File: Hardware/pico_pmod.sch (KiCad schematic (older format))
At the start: 8 parts, among them J1 Conn_02x15_Odd_Even, J2 Conn_01x02, J3 Conn_01x02, J4 Conn_01x02, J5 Conn_01x03, J6 Conn_01x02, J7 Conn_01x05, U1 Pico

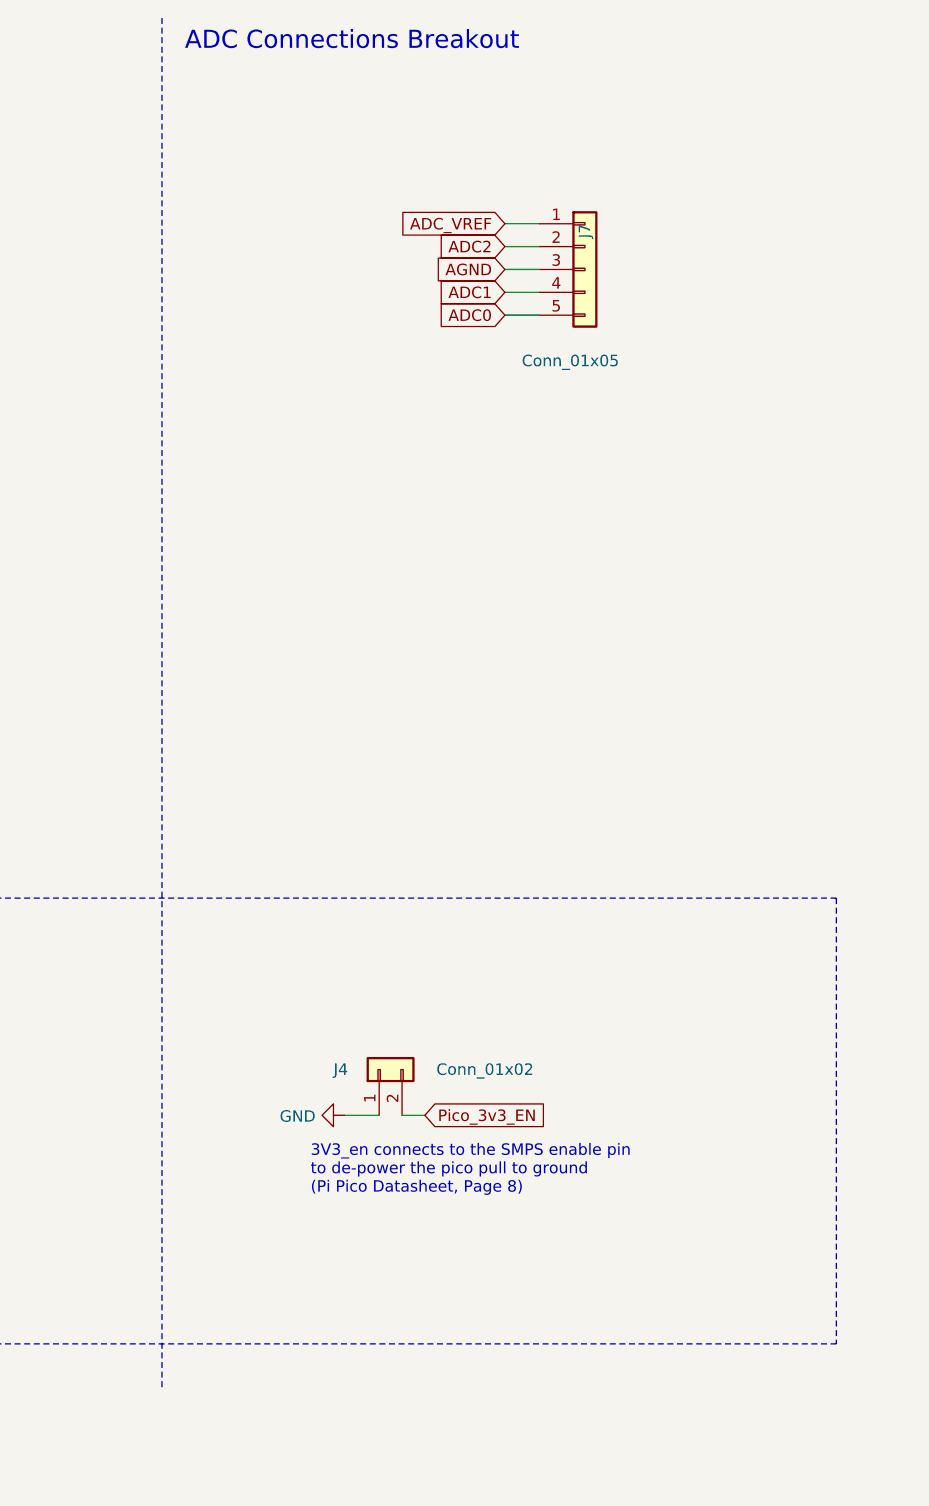
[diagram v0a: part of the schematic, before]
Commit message: Add Reset button to the Pico Schematic
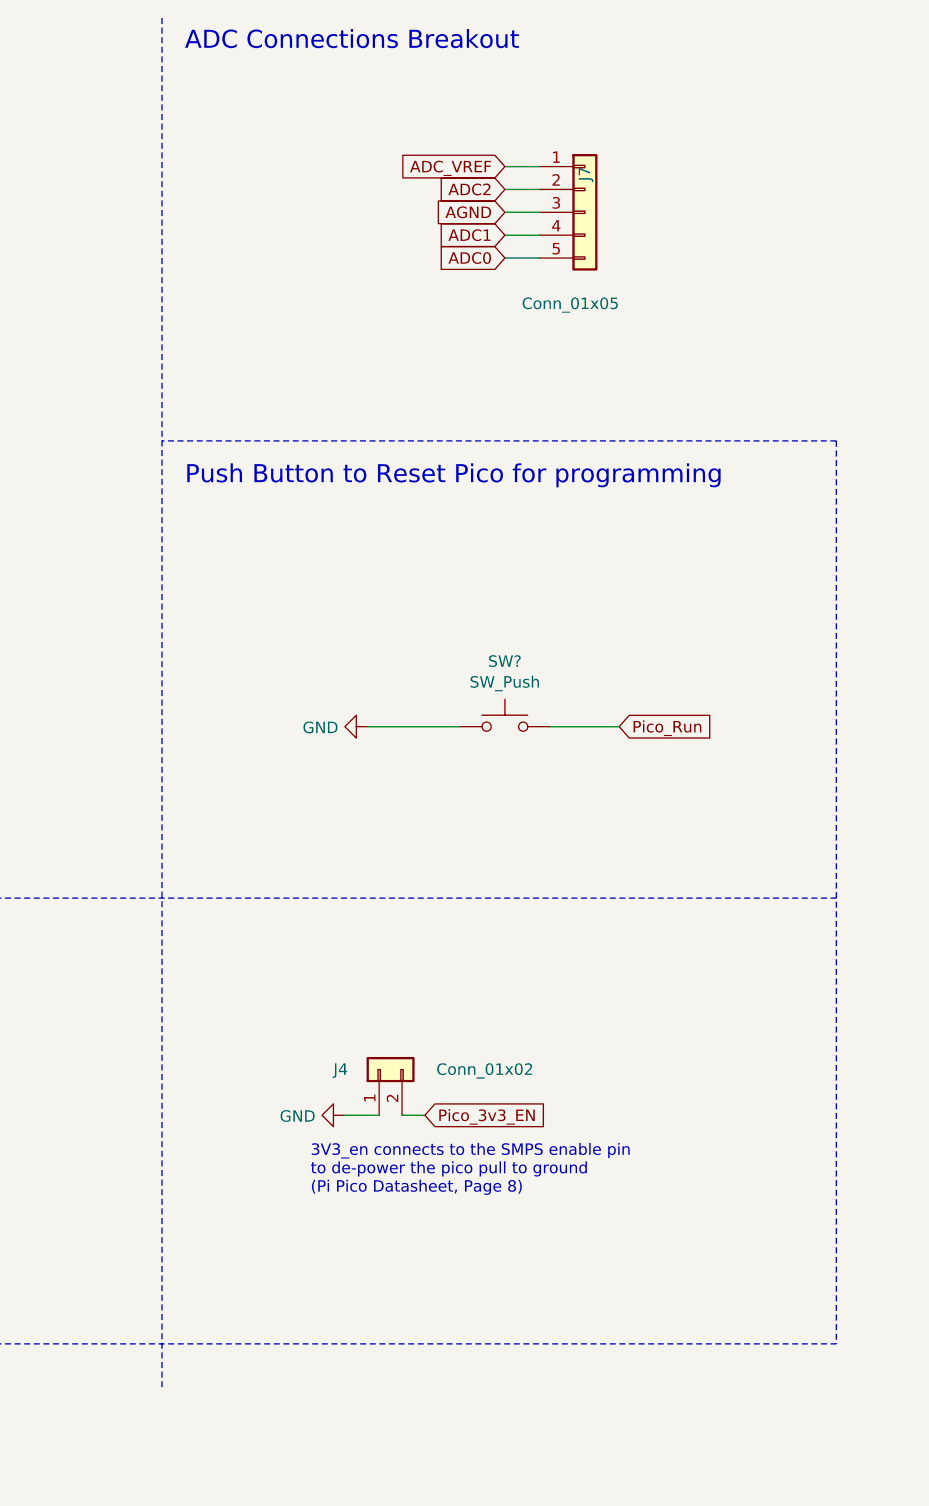
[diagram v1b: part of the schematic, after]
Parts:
- added SW?: SW_Push, Button_Switch_THT:SW_PUSH_6mm_H4.3mm, symbol Switch:SW_Push
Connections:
- net GND: now also SW?.1
- net Pico_Run: now also SW?.2
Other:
- note added: "Push Button to Reset Pico for programming"
- moved on the sheet: J7
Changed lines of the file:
@@
 L Connector_Generic:Conn_01x05 J7
 U 1 1 607A6E5A
-P 10050 1600
-F 0 "J7" V 10050 1800 50  0000 R CNN
-F 1 "Conn_01x05" H 10200 1200 50  0000 R CNN
-F 2 "Connector_PinHeader_2.54mm:PinHeader_1x05_P2.54mm_Vertical" H 10050 1600 50  0001 C CNN
-F 3 "~" H 10050 1600 50  0001 C CNN
-	1    10050 1600
+P 10050 1350
+F 0 "J7" V 10050 1550 50  0000 R CNN
+F 1 "Conn_01x05" H 10200 950 50  0000 R CNN
+F 2 "Connector_PinHeader_2.54mm:PinHeader_1x05_P2.54mm_Vertical" H 10050 1350 50  0001 C CNN
+F 3 "~" H 10050 1350 50  0001 C CNN
+	1    10050 1350
 	1    0    0    -1
 $EndComp
-Text GLabel 9700 1400 0    50   Input ~ 0
+Text GLabel 9700 1150 0    50   Input ~ 0
 ADC_VREF
-Text GLabel 9700 1500 0    50   Input ~ 0
+Text GLabel 9700 1250 0    50   Input ~ 0
 ADC2
-Text GLabel 9700 1600 0    50   Input ~ 0
+Text GLabel 9700 1350 0    50   Input ~ 0
 AGND
-Text GLabel 9700 1700 0    50   Input ~ 0
+Text GLabel 9700 1450 0    50   Input ~ 0
 ADC1
-Text GLabel 9700 1800 0    50   Input ~ 0
+Text GLabel 9700 1550 0    50   Input ~ 0
 ADC0
 Wire Wire Line
-	9700 1400 9850 1400
+	9700 1150 9850 1150
 Wire Wire Line
-	9700 1500 9850 1500
+	9700 1250 9850 1250
 Wire Wire Line
-	9700 1600 9850 1600
+	9700 1350 9850 1350
 Wire Wire Line
-	9850 1700 9700 1700
+	9850 1450 9700 1450
 Wire Wire Line
-	9700 1800 9850 1800
+	9700 1550 9850 1550
 Text GLabel 3300 1950 2    50   Input ~ 0
 ADC_VREF
@@
 	3300 2350 3050 2350
 Wire Notes Line
-	11150 4350 11150 6300
-Wire Notes Line
 	500  6300 11150 6300
 Wire Notes Line
@@
 Text Notes 8300 650  0    79   ~ 0
 ADC Connections Breakout\n
+$Comp
+L Switch:SW_Push SW?
+U 1 1 6081E990
+P 9700 3600
+F 0 "SW?" H 9700 3885 50  0000 C CNN
+F 1 "SW_Push" H 9700 3794 50  0000 C CNN
+F 2 "Button_Switch_THT:SW_PUSH_6mm_H4.3mm" H 9700 3800 50  0001 C CNN
+F 3 "~" H 9700 3800 50  0001 C CNN
+	1    9700 3600
+	1    0    0    -1
+$EndComp
+Text GLabel 10200 3600 2    50   Input ~ 0
+Pico_Run
+$Comp
+L power:GND #PWR?
+U 1 1 60823560
+P 9100 3600
+F 0 "#PWR?" H 9100 3350 50  0001 C CNN
+F 1 "GND" V 9105 3472 50  0000 R CNN
+F 2 "" H 9100 3600 50  0001 C CNN
+F 3 "" H 9100 3600 50  0001 C CNN
+	1    9100 3600
+	0    1    1    0
+$EndComp
+Wire Wire Line
+	9100 3600 9500 3600
+Wire Wire Line
+	9900 3600 10200 3600
+Wire Notes Line
+	11150 2350 8200 2350
+Wire Notes Line
+	11150 2350 11150 6300
+Text Notes 8300 2550 0    79   ~ 0
+Push Button to Reset Pico for programming
 $EndSCHEMATC

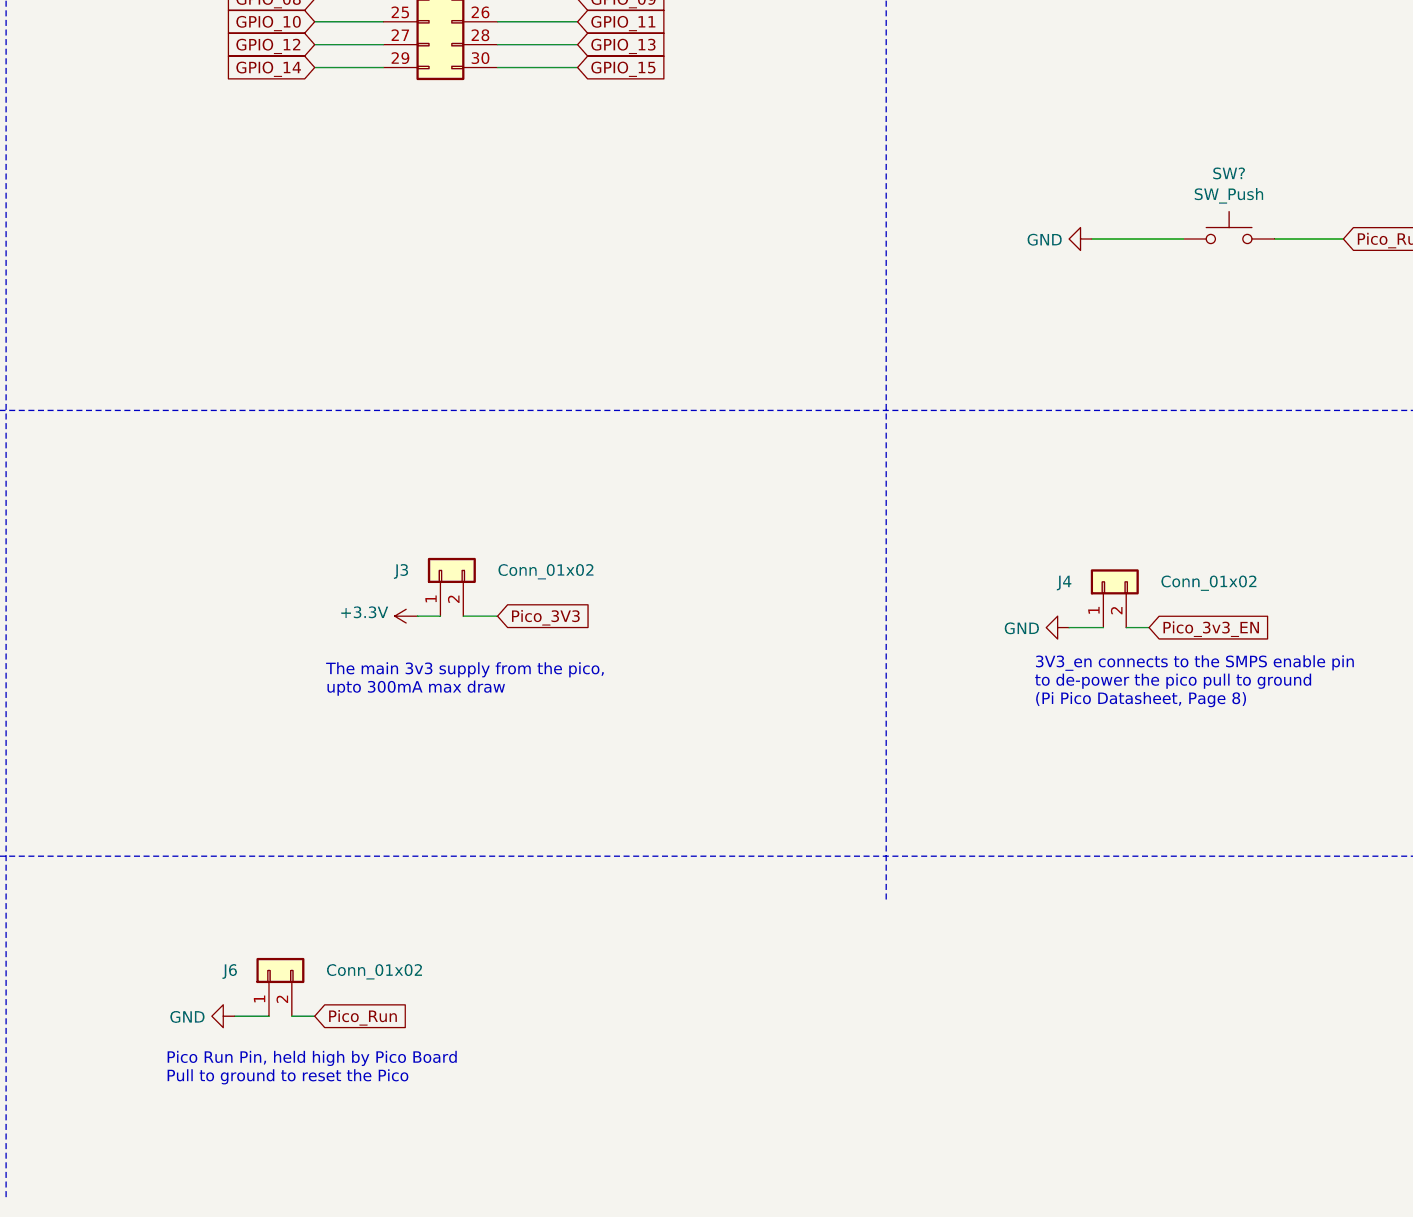
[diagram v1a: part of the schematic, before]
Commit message: Remove Run Header pins
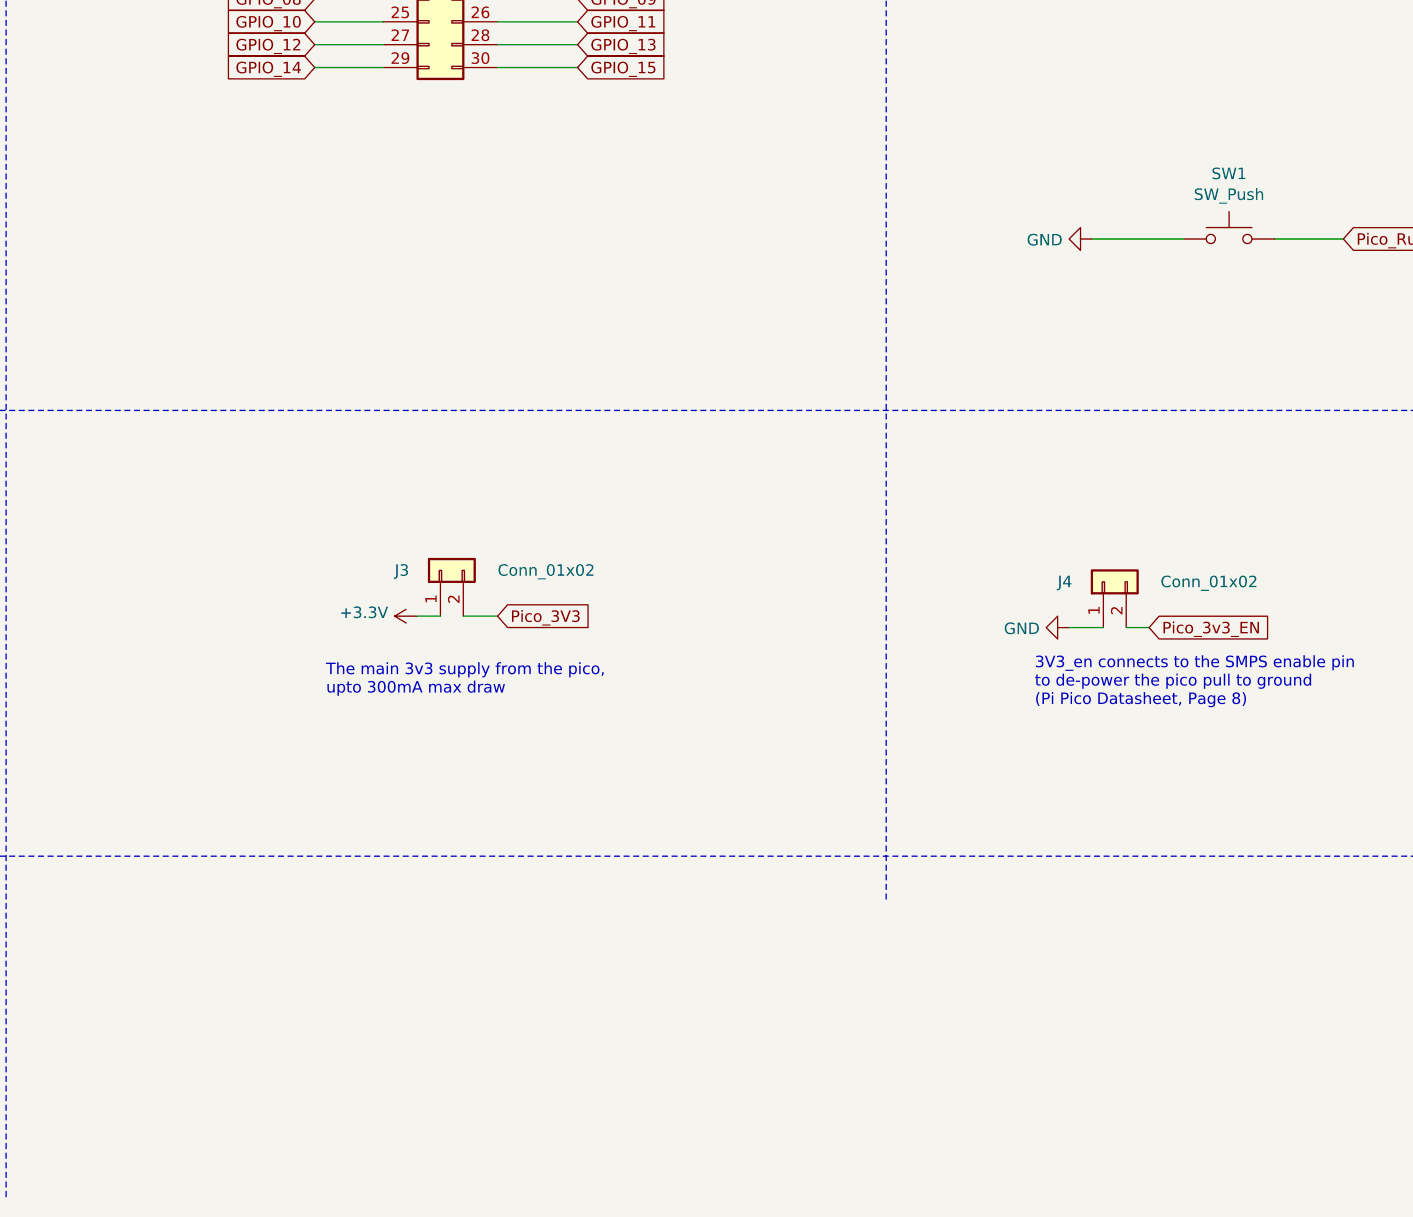
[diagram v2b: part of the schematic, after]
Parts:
- removed J6: Conn_01x02, Connector_PinHeader_2.54mm:PinHeader_1x02_P2.54mm_Vertical, symbol Connector_Generic:Conn_01x02
- gave numbers to parts that had none: 1
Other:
- note removed: "Pico Run Pin, held high by Pico Board\nPull to ground to reset the Pico"
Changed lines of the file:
@@
 Wire Wire Line
 	9150 5300 9000 5300
-Text GLabel 5700 7000 2    50   Input ~ 0
-Pico_Run
-$Comp
-L Connector_Generic:Conn_01x02 J6
-U 1 1 607985C4
-P 5500 6800
-F 0 "J6" V 5500 7000 50  0000 R CNN
-F 1 "Conn_01x02" V 5500 6550 50  0000 R CNN
-F 2 "Connector_PinHeader_2.54mm:PinHeader_1x02_P2.54mm_Vertical" H 5500 6800 50  0001 C CNN
-F 3 "~" H 5500 6800 50  0001 C CNN
-	1    5500 6800
-	0    -1   -1   0
-$EndComp
-Wire Wire Line
-	5600 7000 5700 7000
-Text Notes 5050 7300 0    50   ~ 0
-Pico Run Pin, held high by Pico Board\nPull to ground to reset the Pico
-$Comp
-L power:GND #PWR0124
-U 1 1 607985CC
-P 5350 7000
-F 0 "#PWR0124" H 5350 6750 50  0001 C CNN
-F 1 "GND" V 5355 6872 50  0000 R CNN
-F 2 "" H 5350 7000 50  0001 C CNN
-F 3 "" H 5350 7000 50  0001 C CNN
-	1    5350 7000
-	0    1    1    0
-$EndComp
-Wire Wire Line
-	5500 7000 5350 7000
 Text GLabel 3250 2450 2    50   Input ~ 0
 Pico_Run
@@
 ADC Connections Breakout\n
 $Comp
-L Switch:SW_Push SW?
+L Switch:SW_Push SW1
 U 1 1 6081E990
 P 9700 3600
-F 0 "SW?" H 9700 3885 50  0000 C CNN
+F 0 "SW1" H 9700 3885 50  0000 C CNN
 F 1 "SW_Push" H 9700 3794 50  0000 C CNN
 F 2 "Button_Switch_THT:SW_PUSH_6mm_H4.3mm" H 9700 3800 50  0001 C CNN
@@
 Pico_Run
 $Comp
-L power:GND #PWR?
+L power:GND #PWR0125
 U 1 1 60823560
 P 9100 3600
-F 0 "#PWR?" H 9100 3350 50  0001 C CNN
+F 0 "#PWR0125" H 9100 3350 50  0001 C CNN
 F 1 "GND" V 9105 3472 50  0000 R CNN
 F 2 "" H 9100 3600 50  0001 C CNN
